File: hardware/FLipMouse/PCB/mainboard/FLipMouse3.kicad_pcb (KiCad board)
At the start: 2 copper layers, 61 x 32 mm, 89 parts, among them J1 SJ2-3574A, J2 SJ2-3574A, J3 M50-3900542, J4 Conn_ARM_JTAG_SWD_10, J5 Conn_02x05_Odd_Even, J6 USB_OTG, J7 Conn_01x06, Q1 BC847, Q2 BC847, Q3 BSH108, Q4 BSH108, Q5 Si2301, SW1 SW_Push, SW2 SW_Push, U1 ESP32-WROOM, U2 TSOP4838, U3 LPC11U24FBD, U4 TSR_1-2433, U5 MPXV7007GP, U6 AP2127N-3.3, Y1 JA-12.000-18-DFE

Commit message: Updated PCB, final changes & refinements for v3.1b
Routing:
- net GND: track 280.3 -> 319.1 mm, vias 40 -> 41
- net Net-(C5-Pad2): track 52.2 -> 43.3 mm
- net /IR: track 47.8 -> 46.4 mm
- net /FSR2: track 72.8 -> 71.9 mm
- net /FSR4: track 68.9 -> 68.3 mm
- net /VBUS_SW: track 138.6 -> 138.1 mm, vias 6 -> 7

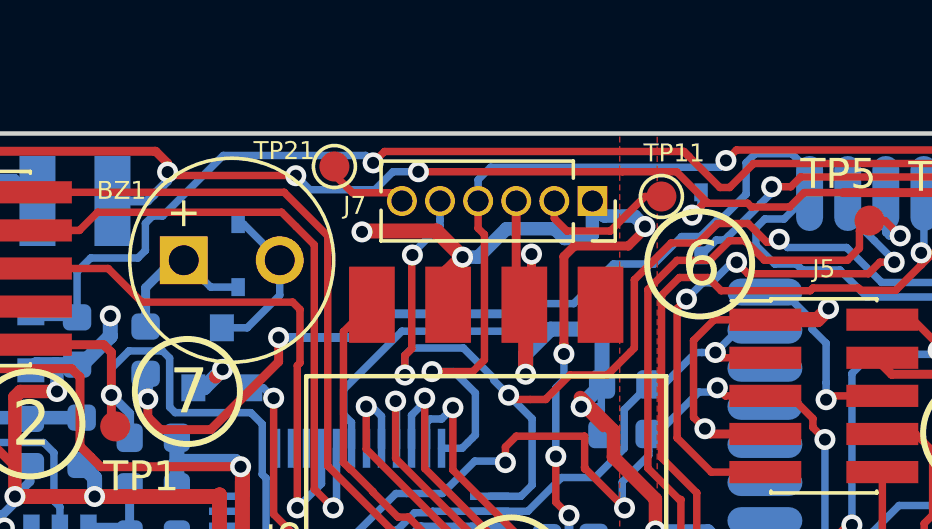
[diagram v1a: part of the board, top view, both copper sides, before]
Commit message: Changed silkscreen size for TP, would be clamped on board edge
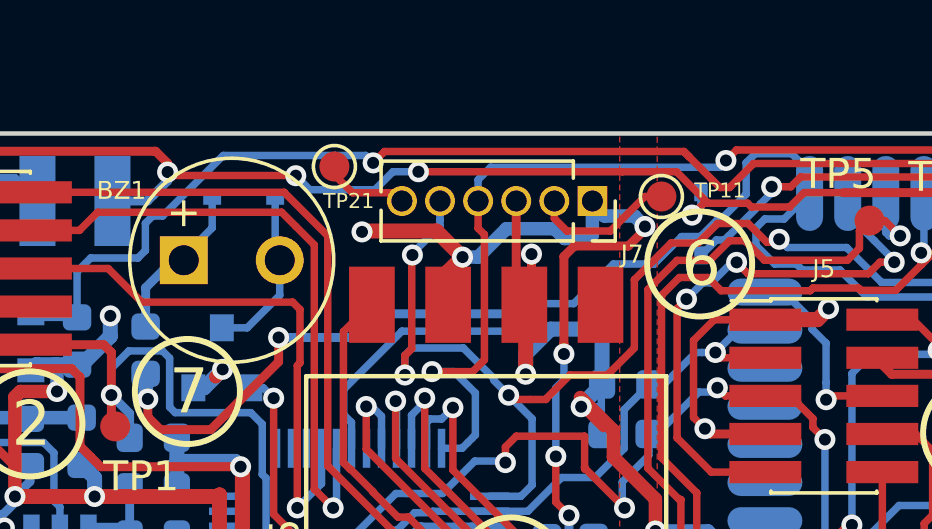
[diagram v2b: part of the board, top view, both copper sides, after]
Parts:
- moved D9 1.93 mm to (73.6, 120.2), turned to 0 degrees
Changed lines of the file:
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@@
     (thickness 1.6)
     (drawings 36)
-    (tracks 1804)
+    (tracks 1805)
     (zones 0)
     (modules 89)
@@
     (descr "Through hole straight socket strip, 1x06, 1.27mm pitch, single row (from Kicad 4.0.7), script generated")
     (tags "Through hole socket strip THT 1x06 1.27mm single row")
-    (fp_text reference J7 (at 0.15 7.925) (layer F.SilkS)
+    (fp_text reference J7 (at 1.775 -1.325) (layer F.SilkS)
       (effects (font (size 0.6 0.6) (thickness 0.15)))
     )
@@
     (tags "test point SMD pad")
     (attr virtual)
-    (fp_text reference TP11 (at 0.425 -1.448) (layer F.SilkS)
-      (effects (font (size 0.6 0.6) (thickness 0.15)))
+    (fp_text reference TP11 (at 1.95 -0.2) (layer F.SilkS)
+      (effects (font (size 0.5 0.5) (thickness 0.125)))
     )
     (fp_text value TP (at 0 1.55) (layer F.Fab)
@@
     (tags "test point SMD pad")
     (attr virtual)
-    (fp_text reference TP21 (at -1.675 -0.525) (layer F.SilkS)
-      (effects (font (size 0.6 0.6) (thickness 0.15)))
+    (fp_text reference TP21 (at 0.475 1.15 180) (layer F.SilkS)
+      (effects (font (size 0.5 0.5) (thickness 0.125)))
     )
     (fp_text value TP (at 0 1.55) (layer F.Fab)
@@
   )
   (module Diode_SMD:D_SOD-323 (layer B.Cu)
-    (at 73.44 122.07 90)
+    (at 73.625 120.15)
     (descr SOD-323)
     (tags SOD-323)
     (attr smd)
-    (fp_text reference D9 (at 2.07 0.06 180) (layer B.SilkS)
+    (fp_text reference D9 (at 2.07 0.06 90) (layer B.SilkS)
       (effects (font (size 0.6 0.6) (thickness 0.15)) (justify mirror))
     )
-    (fp_text value 1N4148WS (at 0.1 -1.9 90) (layer B.Fab)
+    (fp_text value 1N4148WS (at 0.1 -1.9) (layer B.Fab)
       (effects (font (size 1 1) (thickness 0.15)) (justify mirror))
     )
-    (fp_text user %R (at 0 1.85 90) (layer B.Fab)
+    (fp_text user %R (at 0 1.85) (layer B.Fab)
       (effects (font (size 1 1) (thickness 0.15)) (justify mirror))
     )
@@
     (fp_line (start -1.5 -0.85) (end 1.05 -0.85) (layer B.SilkS) (width 0.12))
     (fp_line (start -1.5 0.85) (end 1.05 0.85) (layer B.SilkS) (width 0.12))
-    (pad 1 smd rect (at -1.05 0 90) (size 0.6 0.45) (layers B.Cu B.Paste B.Mask)
+    (pad 1 smd rect (at -1.05 0) (size 0.6 0.45) (layers B.Cu B.Paste B.Mask)
       (net 1 "Net-(BZ1-Pad1)"))
-    (pad 2 smd rect (at 1.05 0 90) (size 0.6 0.45) (layers B.Cu B.Paste B.Mask)
+    (pad 2 smd rect (at 1.05 0) (size 0.6 0.45) (layers B.Cu B.Paste B.Mask)
       (net 2 "Net-(BZ1-Pad2)"))
     (model ${KISYS3DMOD}/Diode_SMD.3dshapes/D_SOD-323.wrl
@@
   (segment (start 70.358 123.142) (end 71.25 122.25) (width 0.3) (layer B.Cu) (net 1))
   (segment (start 70.358 124.4345) (end 70.358 123.142) (width 0.3) (layer B.Cu) (net 1))
-  (segment (start 72.5232 123.12) (end 71.628 122.2248) (width 0.25) (layer B.Cu) (net 1))
-  (segment (start 73.44 123.12) (end 72.5232 123.12) (width 0.25) (layer B.Cu) (net 1))
+  (segment (start 71.628 122.2248) (end 71.628 122.097) (width 0.25) (layer B.Cu) (net 1))
+  (segment (start 72.575 121.15) (end 72.575 120.15) (width 0.25) (layer B.Cu) (net 1))
+  (segment (start 71.628 122.097) (end 72.575 121.15) (width 0.25) (layer B.Cu) (net 1))
   (segment (start 74.828 122.496) (end 74.828 122.2248) (width 0.25) (layer B.Cu) (net 2))
   (segment (start 72.898 124.476) (end 72.898 124.426) (width 0.25) (layer B.Cu) (net 2))
-  (segment (start 73.6232 121.02) (end 74.828 122.2248) (width 0.25) (layer B.Cu) (net 2))
-  (segment (start 73.44 121.02) (end 73.6232 121.02) (width 0.25) (layer B.Cu) (net 2))
   (segment (start 72.898 124.476) (end 73.744 124.476) (width 0.25) (layer B.Cu) (net 2))
   (segment (start 74.828 123.392) (end 74.828 122.2248) (width 0.25) (layer B.Cu) (net 2))
   (segment (start 73.744 124.476) (end 74.828 123.392) (width 0.25) (layer B.Cu) (net 2))
+  (segment (start 74.675 122.0718) (end 74.828 122.2248) (width 0.25) (layer B.Cu) (net 2))
+  (segment (start 74.675 120.15) (end 74.675 122.0718) (width 0.25) (layer B.Cu) (net 2))
   (via (at 98.196279 122.275) (size 0.7) (drill 0.4) (layers F.Cu B.Cu) (net 3))
   (segment (start 97.57 120) (end 97.57 121.801721) (width 0.25) (layer B.Cu) (net 3))
